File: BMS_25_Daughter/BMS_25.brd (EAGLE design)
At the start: 140.3 x 51.7 mm, 178 parts, among them IC1 PBQ79656PAPTQ1, IC2 PBQ79656PAPTQ1, T1 PBHV8115X, 115, T2 PBHV8115X, 115

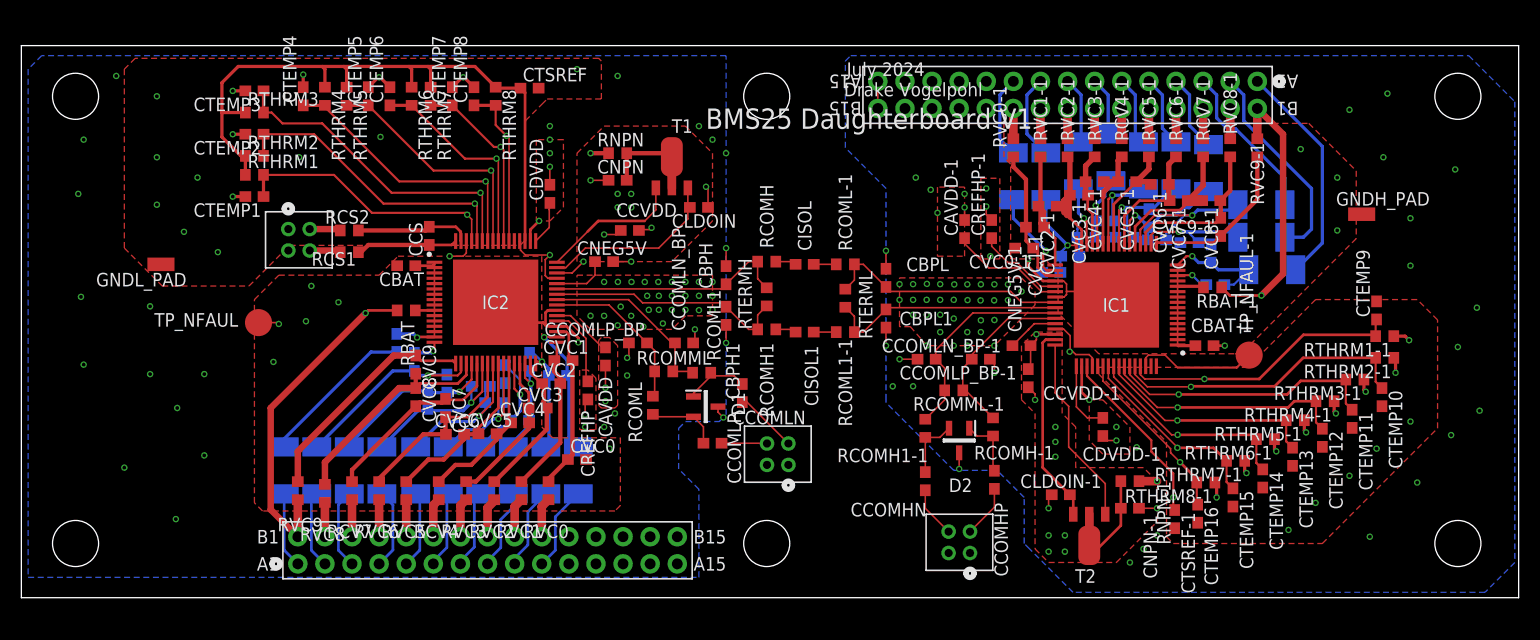
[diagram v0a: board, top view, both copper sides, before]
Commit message: Passed DRC
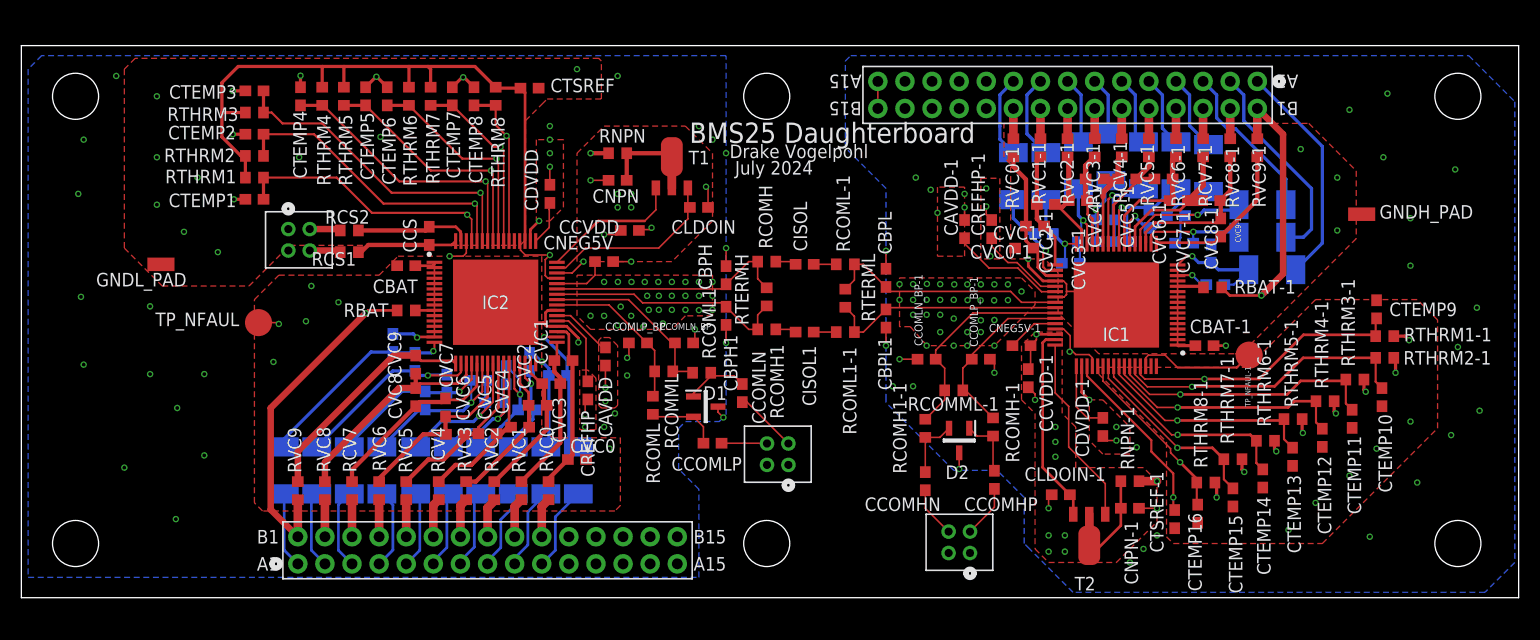
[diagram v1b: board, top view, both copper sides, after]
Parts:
- moved CCB1-1 3.73 mm to (95.8, 34.1)
- moved CCB7-1 2.90 mm to (108.2, 35.8)
- moved CCB3 1.17 mm to (47.4, 17.6)
- moved CCB2-1 0.66 mm to (98.3, 31.3)
- moved CVC6-1 0.62 mm to (107.0, 39.2)
- moved CCB6 0.58 mm to (42.9, 20.4)
- moved CVC3-1 0.52 mm to (99.0, 37.2)
- moved CCB8-1 0.51 mm to (109.0, 33.2)
- moved CCB5-1 0.48 mm to (103.1, 33.4)
- moved CCB3-1 0.41 mm to (99.9, 33.4)
- moved CVC4 0.41 mm to (46.7, 16.0)
- moved CCB10 0.36 mm to (34.8, 23.9)
- moved RTHRM7-1 0.30 mm to (113.5, 13.0)
- moved CCB7 0.26 mm to (37.8, 18.5)
- moved CVC4-1 0.25 mm to (100.6, 39.2)
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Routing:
- net VC2-1: track 14.3 -> 10.5 mm
- net VC1-1: track 12.9 -> 11.0 mm
- net CB0-1: track 11.1 -> 9.26 mm
- net TEMP9: track 71.3 -> 69.9 mm
- net CB6-1: track 12.8 -> 11.7 mm
- net CB7-1: track 16.6 -> 15.8 mm
- net CB1-1: track 8.82 -> 8.00 mm
- net TEMP10: track 75.1 -> 74.4 mm
- net CB6: track 15.9 -> 16.4 mm
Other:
- board text added: "BMS25 Daughterboard"
- board text removed: "BMS25 Daughterboard V1"
